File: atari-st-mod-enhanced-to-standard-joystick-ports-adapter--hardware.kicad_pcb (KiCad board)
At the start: 2 copper layers, 45 parts, among them J1 Joy0/Mouse, J2 Joy1, J3 OLED 128×64, J4 Enhanced Joystick Port, J5 Joy0/Mouse, J6 Joy1, Q1 1<Vgsth<2, Low Rdson, Vds >10, Q10 1<Vgsth<2, Low Rdson, Vds >10, Q2 1<Vgsth<2, Low Rdson, Vds >10, Q3 1<Vgsth<2, Low Rdson, Vds >10, Q4 1<Vgsth<2, Low Rdson, Vds >10, Q5 1<Vgsth<2, Low Rdson, Vds >10, Q6 1<Vgsth<2, Low Rdson, Vds >10, Q7 1<Vgsth<2, Low Rdson, Vds >10, Q8 1<Vgsth<2, Low Rdson, Vds >10, Q9 1<Vgsth<2, Low Rdson, Vds >10, SW1 Reset, SW2 Selector, SW3 Activate/Change, SW4 Cancel, U1 LM4040DBZ-3

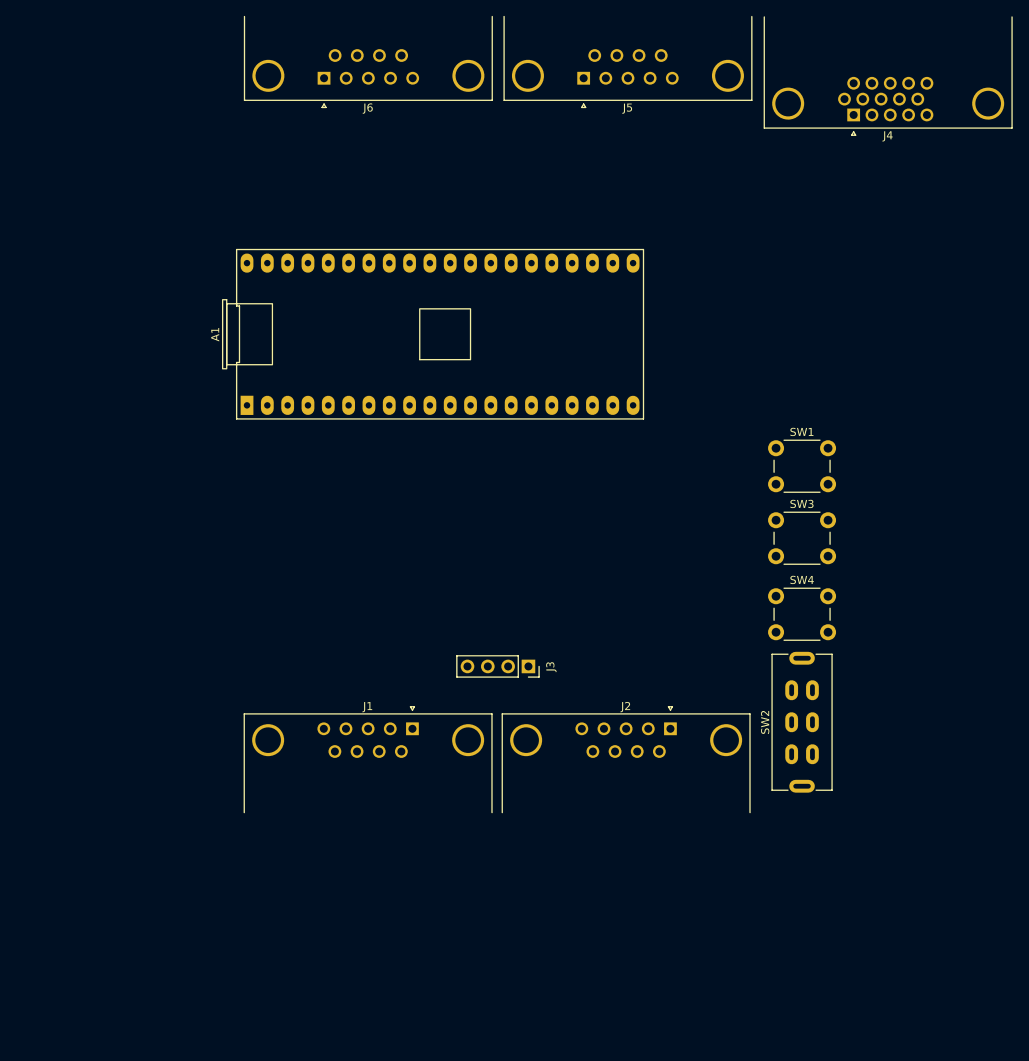
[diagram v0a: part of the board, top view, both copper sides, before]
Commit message: pcb : laying out in a 10x10cm square the big tht components
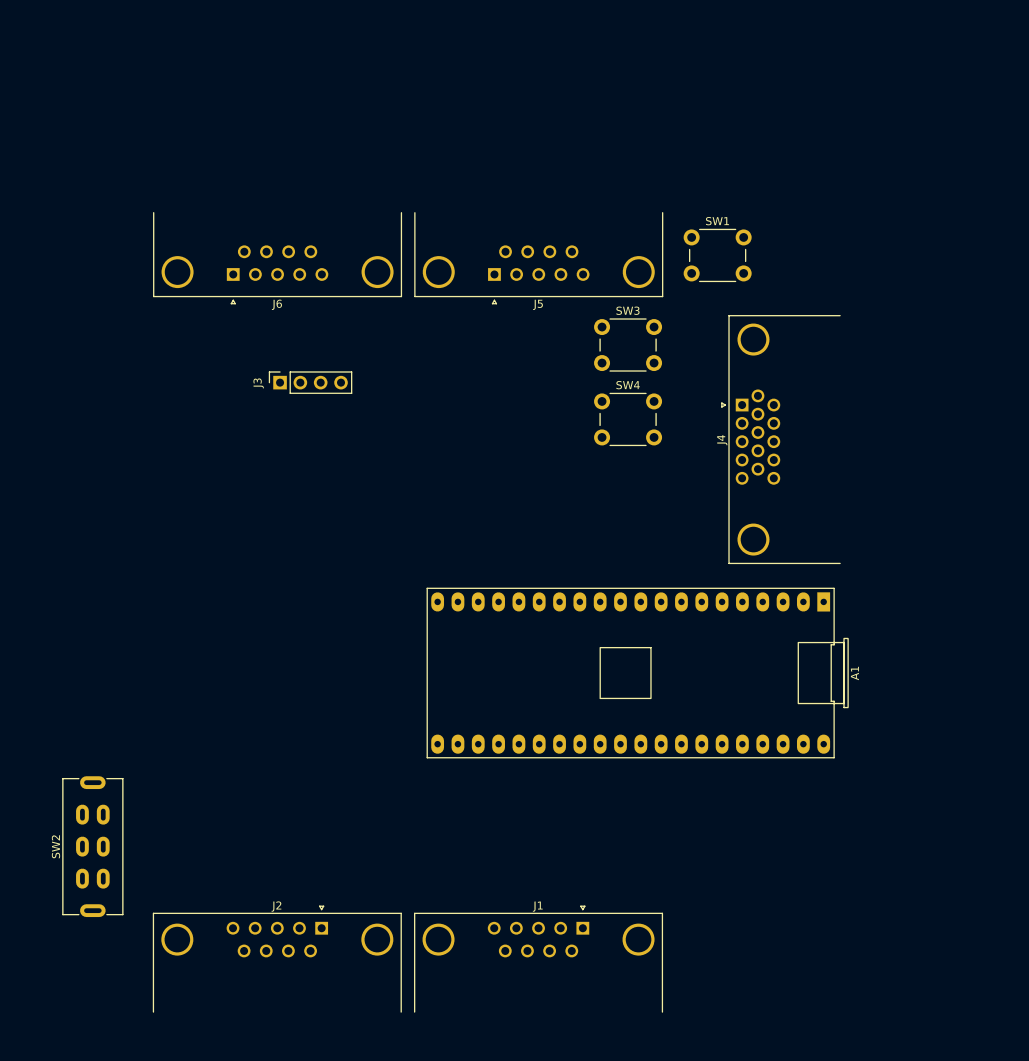
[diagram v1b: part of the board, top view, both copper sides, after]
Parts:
- moved SW2 90.0 mm to (56.6, 129.3)
- moved J2 50.2 mm to (85.2, 139.5)
- moved A1 48.6 mm to (123.8, 107.6), turned to 180 degrees
- moved J3 47.1 mm to (80.0, 71.3), turned to 90 degrees
- moved J4 38.8 mm to (137.8, 74.1), turned to 90 degrees
- moved J1 32.8 mm to (117.8, 139.5)
- moved SW4 32.6 mm to (120.2, 73.7)
- moved SW3 32.5 mm to (120.2, 64.3)
- moved SW1 28.4 mm to (131.4, 53.1)
- moved J6 27.0 mm to (74.2, 57.8)
- moved J5 26.9 mm to (106.8, 57.8)

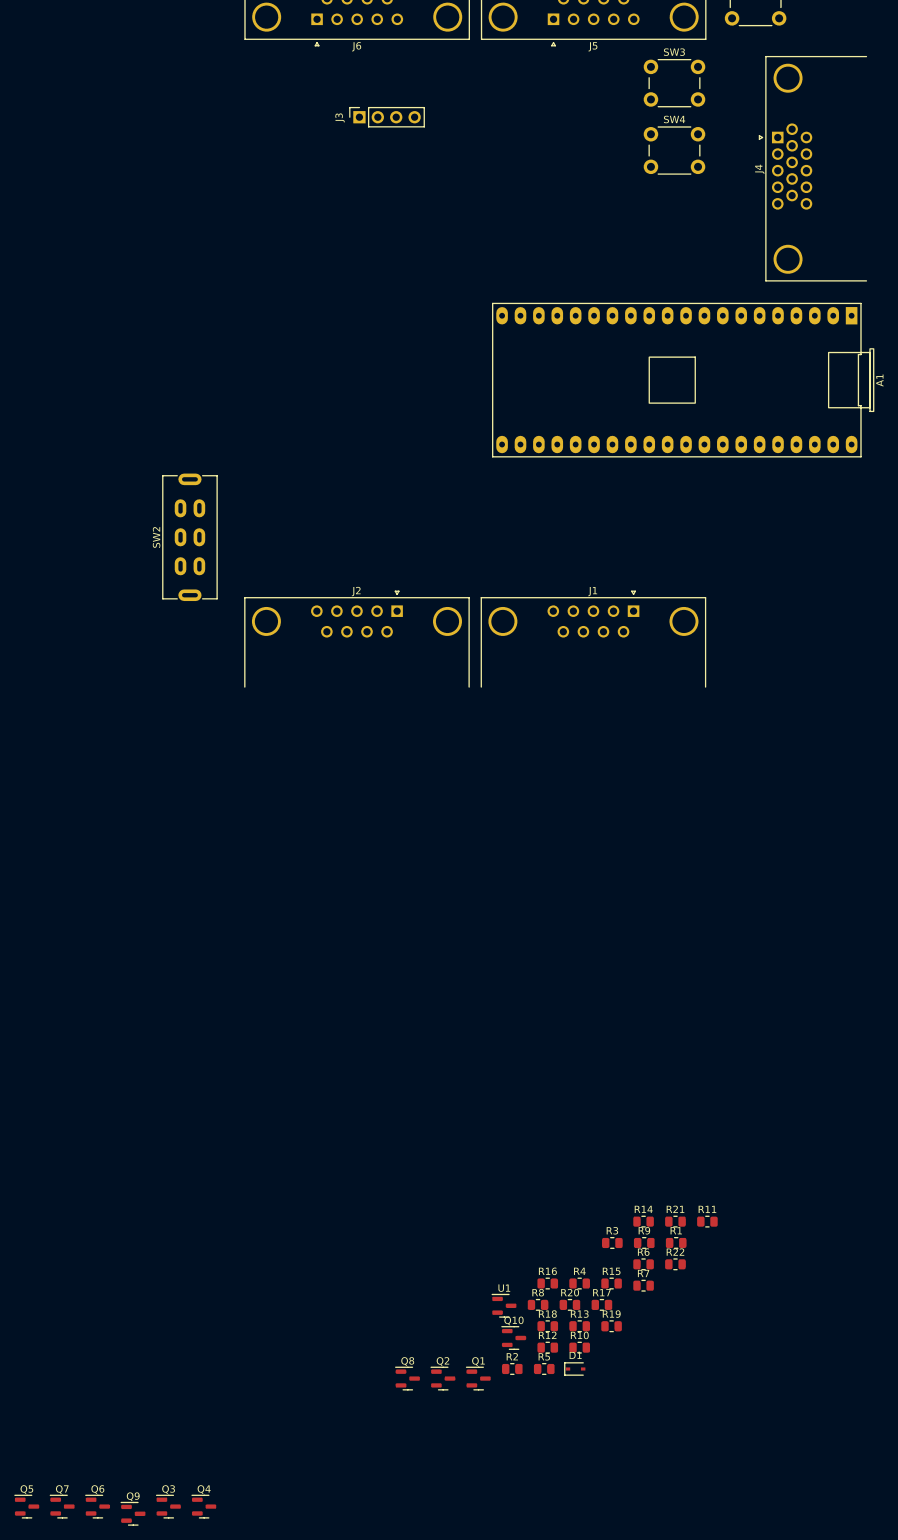
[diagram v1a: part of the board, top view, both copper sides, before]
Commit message: rearrange connexion for easier routing
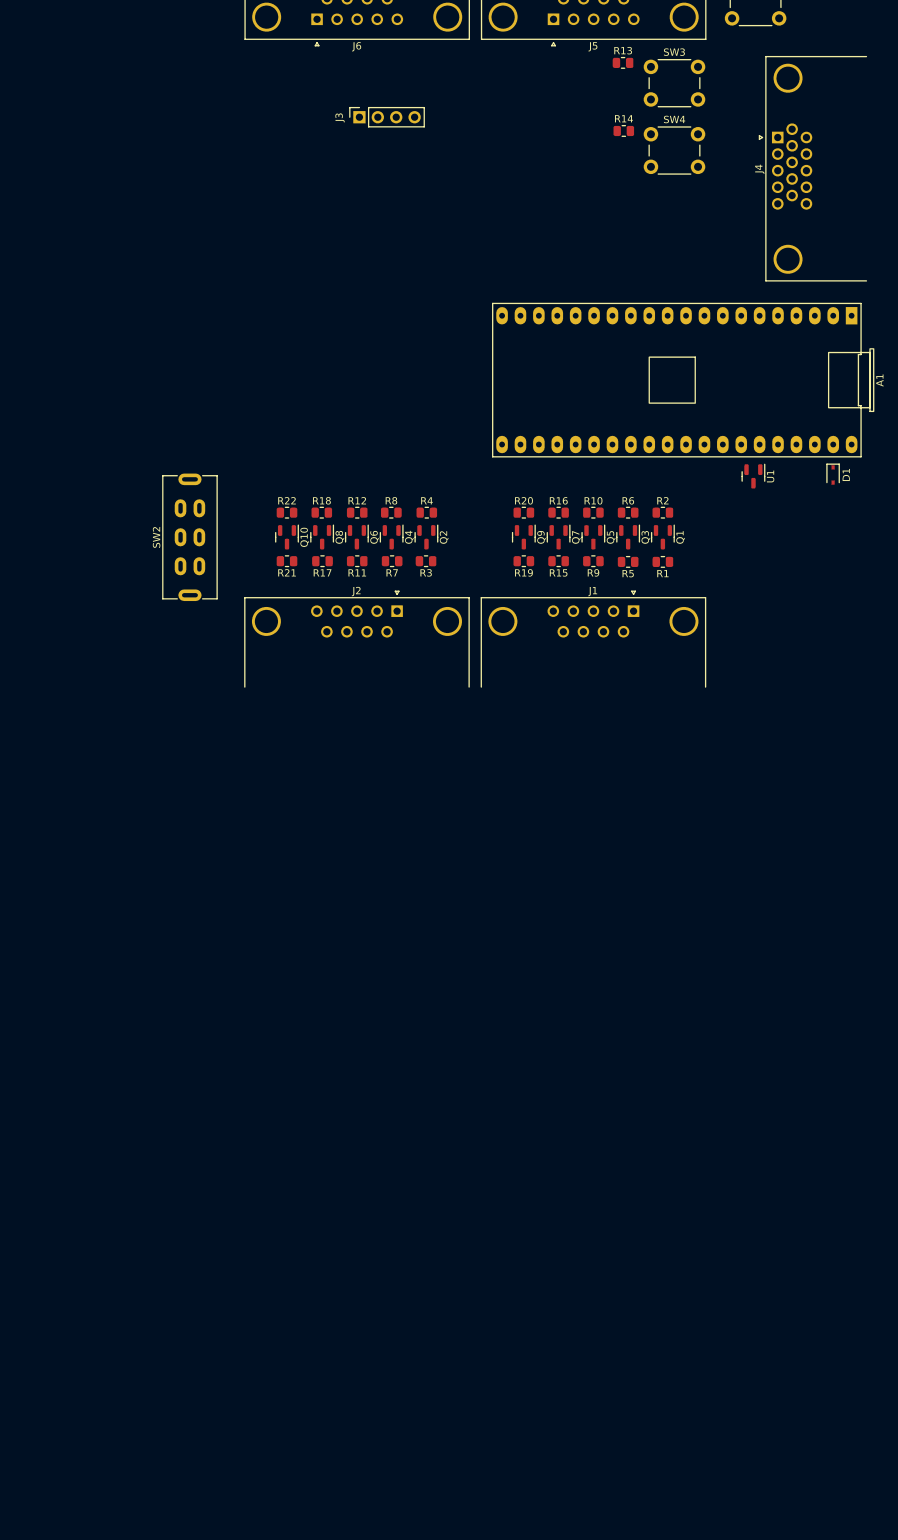
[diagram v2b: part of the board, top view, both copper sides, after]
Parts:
- moved R13 174.5 mm to (116.4, 63.8)
- moved Q5 155.0 mm to (112.3, 129.3), turned to -90 degrees
- moved R14 150.6 mm to (116.5, 73.2)
- moved Q7 150.3 mm to (107.5, 129.3), turned to -90 degrees
- moved Q3 148.1 mm to (117.1, 129.3), turned to -90 degrees
- moved Q9 145.2 mm to (102.7, 129.3), turned to -90 degrees
- moved Q6 138.5 mm to (79.7, 129.3), turned to -90 degrees
- moved Q4 136.3 mm to (84.5, 129.3), turned to -90 degrees
- moved D1 128.5 mm to (145.4, 120.7), turned to -90 degrees
- moved R2 120.0 mm to (121.9, 125.9), turned to 180 degrees
- moved U1 119.6 mm to (134.4, 120.9), turned to -90 degrees
- moved Q1 118.9 mm to (121.9, 129.3), turned to -90 degrees
- moved R12 118.2 mm to (79.7, 125.9), turned to 180 degrees
- moved R22 116.8 mm to (70.0, 125.9), turned to 180 degrees
- moved Q8 116.8 mm to (74.8, 129.3), turned to -90 degrees
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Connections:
- A1 pad 1: /up0 -> /jag_row3
- A1 pad 10: /left1 -> /jag_col2
- A1 pad 11: /right1 -> /jag_col1
- A1 pad 12: /fire1 -> /jag_row1
- A1 pad 14: /button1 -> /button2
- A1 pad 15: /button2 -> /button1
- A1 pad 19: /jag_col1 -> /left1
- A1 pad 2: /down0 -> /jag_row4
- A1 pad 20: /jag_col2 -> /right1
- A1 pad 21: /jag_col3 -> /down1
- A1 pad 22: /jag_col4 -> /fire1
- A1 pad 24: /jag_row1 -> /up1
- A1 pad 25: /jag_row2 -> /right0
- A1 pad 26: /jag_row3 -> /left0
- A1 pad 27: /jag_row4 -> /down0
- A1 pad 29: /jag_row5 -> /fire0
- A1 pad 31: /jag_row6 -> /up0
- A1 pad 4: /left0 -> /jag_row5
- A1 pad 5: /right0 -> /jag_row6
- A1 pad 6: /fire0 -> /jag_row2
- A1 pad 7: /up1 -> /jag_col4
- A1 pad 9: /down1 -> /jag_col3
- Q10 pad 2: /fire1 -> /right1
- Q10 pad 3: /j1_fire -> /j1_right
- Q3 pad 2: /down0 -> /fire0
- Q3 pad 3: /j0_down -> /j0_fire
- Q4 pad 2: /down1 -> /fire1
- Q4 pad 3: /j1_down -> /j1_fire
- Q5 pad 2: /left0 -> /down0
- Q5 pad 3: /j0_left -> /j0_down
- Q6 pad 2: /left1 -> /down1
- Q6 pad 3: /j1_left -> /j1_down
- Q7 pad 2: /right0 -> /left0
- Q7 pad 3: /j0_right -> /j0_left
- Q8 pad 2: /right1 -> /left1
- Q8 pad 3: /j1_right -> /j1_left
- Q9 pad 2: /fire0 -> /right0
- Q9 pad 3: /j0_fire -> /j0_right
- R10 pad 2: /left0 -> /down0
- R11 pad 2: /j1_left -> /j1_down
- R12 pad 2: /left1 -> /down1
- R15 pad 2: /j0_right -> /j0_left
- R16 pad 2: /right0 -> /left0
- R17 pad 2: /j1_right -> /j1_left
- R18 pad 2: /right1 -> /left1
- R19 pad 2: /j0_fire -> /j0_right
- R20 pad 2: /fire0 -> /right0
- R21 pad 2: /j1_fire -> /j1_right
- R22 pad 2: /fire1 -> /right1
- R5 pad 2: /j0_down -> /j0_fire
- R6 pad 2: /down0 -> /fire0
- R7 pad 2: /j1_down -> /j1_fire
- R8 pad 2: /down1 -> /fire1
- R9 pad 2: /j0_left -> /j0_down
